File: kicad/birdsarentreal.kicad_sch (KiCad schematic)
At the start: 29 parts, among them J1 Adafruit Coil Jumper, J2 Adafruit Coil Jumper, J3 Adafruit Coil Jumper, J4 Adafruit Coil Jumper, Q2 NMOS, U12 NCP176AMX330TCG, U9 MCP73831-2-OT

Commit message: So many DRC errors
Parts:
- added F1, F2: Fuse, Fuse:Fuse_0805_2012Metric_Pad1.15x1.40mm_HandSolder, symbol Device:Fuse
- J1, J2, J3, J4, L2: footprint Connector_PinHeader_1.00mm:PinHeader_1x02_P1.00mm_Vertical -> Connector_PinSocket_2.54mm:PinSocket_1x02_P2.54mm_Vertical
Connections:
- net Controller/VBAT: now also F2.2; no longer BT2.1 (+), C10.1, J1.1 (Pin_1), U9.3 (V_{BAT})
- net at C20.1, J2.1 (Pin_1), U7.1 (Vdd)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: now also F1.2; no longer C7.1, D10.1 (K), D11.1 (K)
- new net: BT2.1 (+), C10.1, F2.1, J1.1 (Pin_1), U9.3 (V_{BAT})
- new net: C7.1, D10.1 (K), D11.1 (K), F1.1
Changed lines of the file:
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@@
   (junction (at 187.96 91.44) (diameter 0) (color 0 0 0 0)
-  )
-  (junction (at 135.89 78.74) (diameter 0) (color 0 0 0 0)
   )
   (junction (at 194.31 78.74) (diameter 0) (color 0 0 0 0)
@@
     (stroke (width 0) (type default))
   )
-  (wire (pts (xy 49.53 85.09) (xy 58.42 85.09))
+  (wire (pts (xy 49.53 85.09) (xy 50.8 85.09))
     (stroke (width 0) (type default))
   )
@@
     (stroke (width 0) (type default))
   )
+  (wire (pts (xy 129.54 78.74) (xy 138.43 78.74))
+    (stroke (width 0) (type default))
+  )
   (wire (pts (xy 93.98 101.6) (xy 99.06 101.6))
     (stroke (width 0) (type default))
@@
     (stroke (width 0) (type default))
   )
+  (wire (pts (xy 146.05 78.74) (xy 153.67 78.74))
+    (stroke (width 0) (type default))
+  )
   (wire (pts (xy 40.64 92.71) (xy 40.64 95.25))
     (stroke (width 0) (type default))
@@
     (stroke (width 0) (type default))
   )
-  (wire (pts (xy 129.54 78.74) (xy 135.89 78.74))
-    (stroke (width 0) (type default))
-  )
   (wire (pts (xy 13.97 85.09) (xy 21.59 85.09))
     (stroke (width 0) (type default))
@@
     (stroke (width 0) (type default))
   )
-  (wire (pts (xy 135.89 78.74) (xy 135.89 63.5))
+  (wire (pts (xy 153.67 78.74) (xy 153.67 63.5))
     (stroke (width 0) (type default))
   )
@@
     (stroke (width 0) (type default))
   )
-  (wire (pts (xy 135.89 78.74) (xy 153.67 78.74))
-    (stroke (width 0) (type default))
-  )
   (wire (pts (xy 129.54 86.36) (xy 135.89 86.36))
     (stroke (width 0) (type default))
   )
-  (wire (pts (xy 135.89 63.5) (xy 205.74 63.5))
+  (wire (pts (xy 153.67 63.5) (xy 205.74 63.5))
     (stroke (width 0) (type default))
   )
@@
         (path "/9f6eb88e-d254-4b8d-b64f-838940a89234/50902c9c-c184-4e8b-b7c8-1add935d161c"
           (reference "C9") (unit 1)
+        )
+      )
+    )
+  )
+  (symbol (lib_id "Device:Fuse") (at 142.24 78.74 90) (unit 1)
+    (in_bom yes) (on_board yes) (dnp no) (fields_autoplaced)
+    (property "Reference" "F2" (at 142.24 73.66 90)
+      (effects (font (size 1.27 1.27)))
+    )
+    (property "Value" "Fuse" (at 142.24 76.2 90)
+      (effects (font (size 1.27 1.27)))
+    )
+    (property "Footprint" "Fuse:Fuse_0805_2012Metric_Pad1.15x1.40mm_HandSolder" (at 142.24 80.518 90)
+      (effects (font (size 1.27 1.27)) hide)
+    )
+    (property "Datasheet" "~" (at 142.24 78.74 0)
+      (effects (font (size 1.27 1.27)) hide)
+    )
+    (pin "1")
+    (pin "2")
+    (instances
+      (project "robot"
+        (path "/9f6eb88e-d254-4b8d-b64f-838940a89234/50902c9c-c184-4e8b-b7c8-1add935d161c"
+          (reference "F2") (unit 1)
         )
       )
@@
       (effects (font (size 1.27 1.27)))
     )
-    (property "Footprint" "Connector_PinHeader_1.00mm:PinHeader_1x02_P1.00mm_Vertical" (at 214.63 119.38 0)
+    (property "Footprint" "Connector_PinSocket_2.54mm:PinSocket_1x02_P2.54mm_Vertical" (at 214.63 119.38 0)
       (effects (font (size 1.27 1.27)) hide)
     )
@@
     )
   )
+  (symbol (lib_id "Device:Fuse") (at 54.61 85.09 90) (unit 1)
+    (in_bom yes) (on_board yes) (dnp no) (fields_autoplaced)
+    (property "Reference" "F1" (at 54.61 80.01 90)
+      (effects (font (size 1.27 1.27)))
+    )
+    (property "Value" "Fuse" (at 54.61 82.55 90)
+      (effects (font (size 1.27 1.27)))
+    )
+    (property "Footprint" "Fuse:Fuse_0805_2012Metric_Pad1.15x1.40mm_HandSolder" (at 54.61 86.868 90)
+      (effects (font (size 1.27 1.27)) hide)
+    )
+    (property "Datasheet" "~" (at 54.61 85.09 0)
+      (effects (font (size 1.27 1.27)) hide)
+    )
+    (pin "1")
+    (pin "2")
+    (instances
+      (project "robot"
+        (path "/9f6eb88e-d254-4b8d-b64f-838940a89234/50902c9c-c184-4e8b-b7c8-1add935d161c"
+          (reference "F1") (unit 1)
+        )
+      )
+    )
+  )
   (symbol (lib_id "Device:C") (at 194.31 82.55 0) (unit 1)
     (in_bom yes) (on_board yes) (dnp no) (fields_autoplaced)
@@
       (effects (font (size 1.27 1.27)))
     )
-    (property "Footprint" "Connector_PinHeader_1.00mm:PinHeader_1x02_P1.00mm_Vertical" (at 46.99 107.95 0)
+    (property "Footprint" "Connector_PinSocket_2.54mm:PinSocket_1x02_P2.54mm_Vertical" (at 46.99 107.95 0)
       (effects (font (size 1.27 1.27)) hide)
     )
@@
       (effects (font (size 1.27 1.27)) (justify right))
     )
-    (property "Footprint" "Connector_PinHeader_1.00mm:PinHeader_1x02_P1.00mm_Vertical" (at 13.97 88.9 0)
+    (property "Footprint" "Connector_PinSocket_2.54mm:PinSocket_1x02_P2.54mm_Vertical" (at 13.97 88.9 0)
       (effects (font (size 1.27 1.27)) hide)
     )
@@
       (effects (font (size 1.27 1.27)))
     )
-    (property "Footprint" "Connector_PinHeader_1.00mm:PinHeader_1x02_P1.00mm_Vertical" (at 80.01 107.95 0)
+    (property "Footprint" "Connector_PinSocket_2.54mm:PinSocket_1x02_P2.54mm_Vertical" (at 80.01 107.95 0)
       (effects (font (size 1.27 1.27)) hide)
     )
@@
       (effects (font (size 1.27 1.27)))
     )
-    (property "Footprint" "Connector_PinHeader_1.00mm:PinHeader_1x02_P1.00mm_Vertical" (at 137.16 113.03 0)
-      (effects (font (size 1.27 1.27)) hide)
-    )
+    (property "Footprint" "Connector_PinSocket_2.54mm:PinSocket_1x02_P2.54mm_Vertical" (at 137.16 113.03 0)
+      (effects (font (size 1.27 1.27)) hide)
+    )

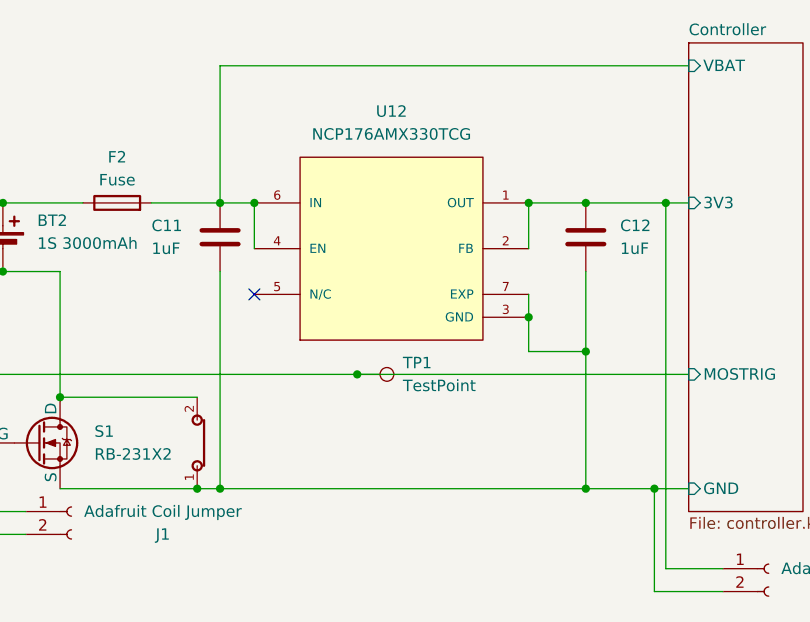
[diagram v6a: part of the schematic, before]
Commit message: Add new 3.3V regulator
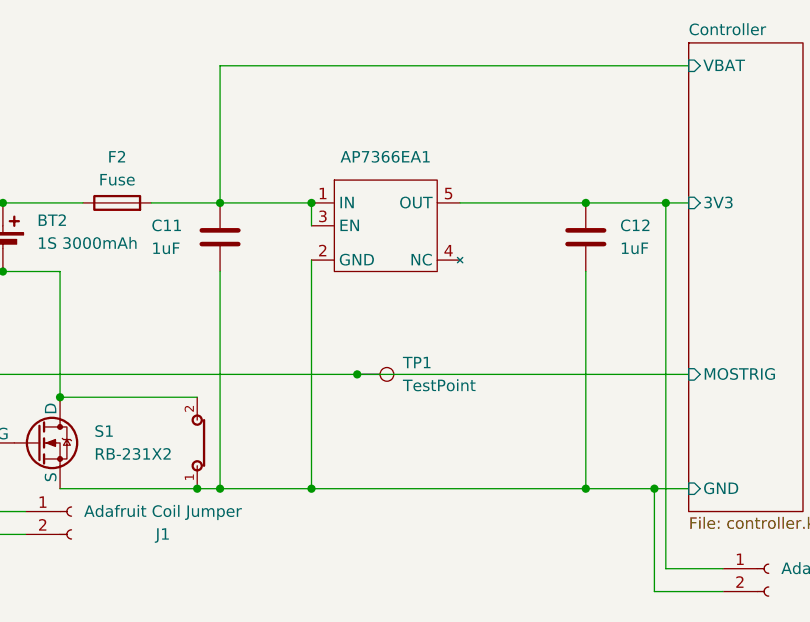
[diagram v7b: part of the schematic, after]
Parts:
- removed U12: NCP176AMX330TCG, NCP176AMX330TCG:PSON40P120X120X45-7N_NCP176AMX330TCG, symbol NCP176AMX330TCG:NCP176AMX330TCG
- added AP7366EA1: ~, Package_TO_SOT_SMD:SOT-23-5_HandSoldering, symbol AP7366EA-33W5-7:AP7366EA-33W5-7
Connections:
- net Controller/3V3: now also AP7366EA1.5 (OUT)
- net Controller/GND: now also AP7366EA1.2 (GND)
- net Controller/VBAT: now also AP7366EA1.1 (IN), AP7366EA1.3 (EN)
- no-connect marks 1 -> 0

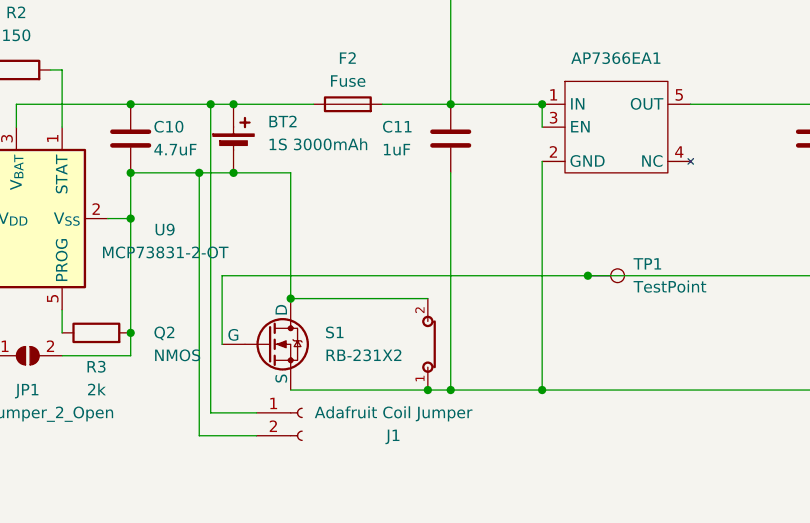
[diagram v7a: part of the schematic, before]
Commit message: Add tilt switch
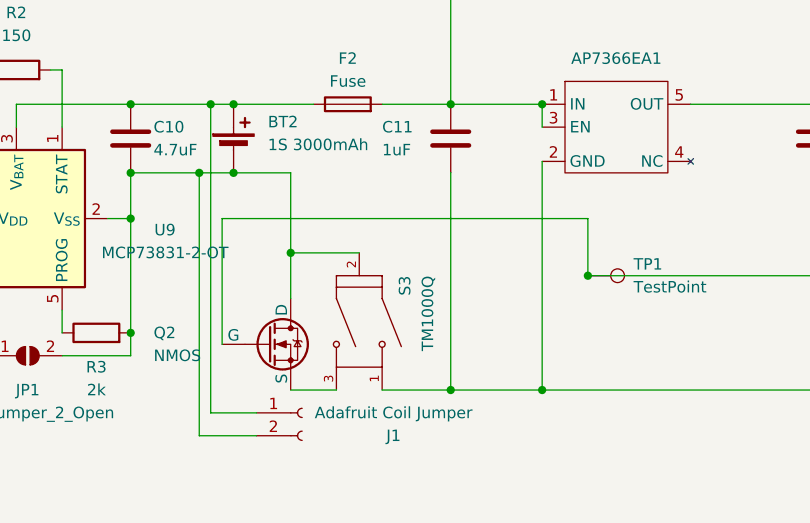
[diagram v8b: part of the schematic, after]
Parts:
- removed S1: RB-231X2, RB-231X2:SW_RB-231X2, symbol RB-231X2:RB-231X2
- added S3: TM1000Q, TM1000Q:SW_TM1000Q, symbol TM1000Q:TM1000Q
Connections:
- net Controller/GND: now also S3.1; no longer Q2.3 (S)
- net at BT2.2 (-), C10.2, J1.2 (Pin_2)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: now also S3.2
- new net: Q2.3 (S), S3.3
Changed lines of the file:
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@@
   (junction (at 163.83 110.49) (diameter 0) (color 0 0 0 0)
   )
-  (junction (at 135.89 100.33) (diameter 0) (color 0 0 0 0)
-  )
   (junction (at 118.11 104.14) (diameter 0) (color 0 0 0 0)
   )
@@
   (junction (at 80.01 101.6) (diameter 0) (color 0 0 0 0)
   )
+  (junction (at 135.89 95.25) (diameter 0) (color 0 0 0 0)
+  )
   (junction (at 93.98 101.6) (diameter 0) (color 0 0 0 0)
   )
@@
   (junction (at 201.93 110.49) (diameter 0) (color 0 0 0 0)
   )
-  (junction (at 151.13 110.49) (diameter 0) (color 0 0 0 0)
-  )
   (junction (at 40.64 92.71) (diameter 0) (color 0 0 0 0)
   )
@@
     (stroke (width 0) (type default))
   )
-  (wire (pts (xy 135.89 100.33) (xy 151.13 100.33))
-    (stroke (width 0) (type default))
-  )
   (wire (pts (xy 82.55 85.09) (xy 82.55 92.71))
     (stroke (width 0) (type default))
@@
     (stroke (width 0) (type default))
   )
-  (wire (pts (xy 128.27 97.79) (xy 168.91 97.79))
+  (wire (pts (xy 128.27 91.44) (xy 168.91 91.44))
     (stroke (width 0) (type default))
   )
@@
     (stroke (width 0) (type default))
   )
-  (wire (pts (xy 128.27 97.79) (xy 128.27 105.41))
+  (wire (pts (xy 128.27 91.44) (xy 128.27 105.41))
     (stroke (width 0) (type default))
   )
@@
     (stroke (width 0) (type default))
   )
+  (wire (pts (xy 135.89 95.25) (xy 135.89 100.33))
+    (stroke (width 0) (type default))
+  )
   (wire (pts (xy 13.97 85.09) (xy 21.59 85.09))
     (stroke (width 0) (type default))
@@
     (stroke (width 0) (type default))
   )
+  (wire (pts (xy 168.91 91.44) (xy 168.91 97.79))
+    (stroke (width 0) (type default))
+  )
   (wire (pts (xy 57.15 101.6) (xy 57.15 105.41))
     (stroke (width 0) (type default))
@@
     (stroke (width 0) (type default))
   )
-  (wire (pts (xy 151.13 110.49) (xy 153.67 110.49))
+  (wire (pts (xy 146.05 110.49) (xy 153.67 110.49))
     (stroke (width 0) (type default))
   )
@@
     (stroke (width 0) (type default))
   )
+  (wire (pts (xy 135.89 95.25) (xy 143.51 95.25))
+    (stroke (width 0) (type default))
+  )
   (wire (pts (xy 62.23 101.6) (xy 80.01 101.6))
     (stroke (width 0) (type default))
@@
     (stroke (width 0) (type default))
   )
-  (wire (pts (xy 135.89 110.49) (xy 151.13 110.49))
+  (wire (pts (xy 135.89 110.49) (xy 140.97 110.49))
     (stroke (width 0) (type default))
   )
@@
     (stroke (width 0) (type default))
   )
-  (wire (pts (xy 135.89 86.36) (xy 135.89 100.33))
+  (wire (pts (xy 135.89 86.36) (xy 135.89 95.25))
     (stroke (width 0) (type default))
   )
   (wire (pts (xy 85.09 107.95) (xy 91.44 107.95))
     (stroke (width 0) (type default))
+  )
+  (symbol (lib_id "TM1000Q:TM1000Q") (at 143.51 102.87 270) (unit 1)
+    (in_bom yes) (on_board yes) (dnp no)
+    (property "Reference" "S3" (at 148.59 97.79 0)
+      (effects (font (size 1.27 1.27)) (justify left))
+    )
+    (property "Value" "TM1000Q" (at 151.13 97.79 0)
+      (effects (font (size 1.27 1.27)) (justify left))
+    )
+    (property "Footprint" "TM1000Q:SW_TM1000Q" (at 143.51 102.87 0)
+      (effects (font (size 1.27 1.27)) (justify bottom) hide)
+    )
+    (property "Datasheet" "" (at 143.51 102.87 0)
+      (effects (font (size 1.27 1.27)) hide)
+    )
+    (property "MF" "E-Switch" (at 143.51 102.87 0)
+      (effects (font (size 1.27 1.27)) (justify bottom) hide)
+    )
+    (property "MAXIMUM_PACKAGE_HEIGHT" "6.5mm" (at 143.51 102.87 0)
+      (effects (font (size 1.27 1.27)) (justify bottom) hide)
+    )
+    (property "Package" "SIP-3 E-Switch" (at 143.51 102.87 0)
+      (effects (font (size 1.27 1.27)) (justify bottom) hide)
+    )
+    (property "Price" "None" (at 143.51 102.87 0)
+      (effects (font (size 1.27 1.27)) (justify bottom) hide)
+    )
+    (property "Check_prices" "https://www.snapeda.com/parts/TM1000Q/E-Switch/view-part/?ref=eda" (at 143.51 102.87 0)
+      (effects (font (size 1.27 1.27)) (justify bottom) hide)
+    )
+    (property "STANDARD" "Manufacturer Recommendations" (at 143.51 102.87 0)
+      (effects (font (size 1.27 1.27)) (justify bottom) hide)
+    )
+    (property "PARTREV" "-" (at 143.51 102.87 0)
+      (effects (font (size 1.27 1.27)) (justify bottom) hide)
+    )
+    (property "SnapEDA_Link" "https://www.snapeda.com/parts/TM1000Q/E-Switch/view-part/?ref=snap" (at 143.51 102.87 0)
+      (effects (font (size 1.27 1.27)) (justify bottom) hide)
+    )
+    (property "MP" "TM1000Q" (at 143.51 102.87 0)
+      (effects (font (size 1.27 1.27)) (justify bottom) hide)
+    )
+    (property "Purchase-URL" "https://www.snapeda.com/api/url_track_click_mouser/?unipart_id=649122&manufacturer=E-Switch&part_name=TM1000Q&search_term=tm1000q" (at 143.51 102.87 0)
+      (effects (font (size 1.27 1.27)) (justify bottom) hide)
+    )
+    (property "Description" "\nSWITCH TILT SPST\n" (at 143.51 102.87 0)
+      (effects (font (size 1.27 1.27)) (justify bottom) hide)
+    )
+    (property "MANUFACTURER" "E-Switch" (at 143.51 102.87 0)
+      (effects (font (size 1.27 1.27)) (justify bottom) hide)
+    )
+    (property "Availability" "In Stock" (at 143.51 102.87 0)
+      (effects (font (size 1.27 1.27)) (justify bottom) hide)
+    )
+    (property "SNAPEDA_PN" "TM1000Q" (at 143.51 102.87 0)
+      (effects (font (size 1.27 1.27)) (justify bottom) hide)
+    )
+    (pin "1")
+    (pin "2")
+    (pin "3")
+    (instances
+      (project "robot"
+        (path "/9f6eb88e-d254-4b8d-b64f-838940a89234/50902c9c-c184-4e8b-b7c8-1add935d161c"
+          (reference "S3") (unit 1)
+        )
+      )
+    )
   )
   (symbol (lib_id "Device:C") (at 93.98 96.52 0) (unit 1)
@@
         )
       )
-    )
-  )
-  (symbol (lib_id "RB-231X2:RB-231X2") (at 151.13 105.41 270) (unit 1)
-    (in_bom yes) (on_board yes) (dnp no)
-    (property "Reference" "S1" (at 139.7 104.14 90)
-      (effects (font (size 1.27 1.27)) (justify left))
-    )
-    (property "Value" "RB-231X2" (at 139.7 106.68 90)
-      (effects (font (size 1.27 1.27)) (justify left))
-    )
-    (property "Footprint" "RB-231X2:SW_RB-231X2" (at 151.13 105.41 0)
-      (effects (font (size 1.27 1.27)) (justify bottom) hide)
-    )
-    (property "Datasheet" "" (at 151.13 105.41 0)
-      (effects (font (size 1.27 1.27)) hide)
-    )
-    (property "MF" "C&K" (at 151.13 105.41 0)
-      (effects (font (size 1.27 1.27)) (justify bottom) hide)
-    )
-    (property "Description" "\nRolling Ball Tilt Switches\n" (at 151.13 105.41 0)
-      (effects (font (size 1.27 1.27)) (justify bottom) hide)
-    )
-    (property "Package" "Radial Side View  C&amp;K Components" (at 151.13 105.41 0)
-      (effects (font (size 1.27 1.27)) (justify bottom) hide)
-    )
-    (property "Price" "None" (at 151.13 105.41 0)
-      (effects (font (size 1.27 1.27)) (justify bottom) hide)
-    )
-    (property "Check_prices" "https://www.snapeda.com/parts/RB-231X2/C%2526K/view-part/?ref=eda" (at 151.13 105.41 0)
-      (effects (font (size 1.27 1.27)) (justify bottom) hide)
-    )
-    (property "SnapEDA_Link" "https://www.snapeda.com/parts/RB-231X2/C%2526K/view-part/?ref=snap" (at 151.13 105.41 0)
-      (effects (font (size 1.27 1.27)) (justify bottom) hide)
-    )
-    (property "MP" "RB-231X2" (at 151.13 105.41 0)
-      (effects (font (size 1.27 1.27)) (justify bottom) hide)
-    )
-    (property "Purchase-URL" "https://www.snapeda.com/api/url_track_click_mouser/?unipart_id=494671&manufacturer=C&amp;K&part_name=RB-231X2&search_term=rb231" (at 151.13 105.41 0)
-      (effects (font (size 1.27 1.27)) (justify bottom) hide)
-    )
-    (property "Availability" "In Stock" (at 151.13 105.41 0)
-      (effects (font (size 1.27 1.27)) (justify bottom) hide)
-    )
-    (property "MANUFACTURER" "CnK" (at 151.13 105.41 0)
-      (effects (font (size 1.27 1.27)) (justify bottom) hide)
-    )
-    (pin "1")
-    (pin "2")
-    (instances
-      (project "robot"
-        (path "/9f6eb88e-d254-4b8d-b64f-838940a89234/50902c9c-c184-4e8b-b7c8-1add935d161c"
-          (reference "S1") (unit 1)
-        )
-      )
